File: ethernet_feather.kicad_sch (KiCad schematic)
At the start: 53 parts, among them J1 USB_C_Receptacle_USB2.0, J2 TC2030-NL, J3 JST PH 2 pin, J4 JST SH4 pin, J4 RJ45_Abracon_ARJM11D7-114-AB-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, J5 Conn_02x02_Odd_Even, U1 MIMXRT1051CVJ5B, U2 LP3982IMM-3.3, U3 MCP73831-2-OT, U4 W25Q32JVZP, U5 WE-TVS-82400102, Y1 24MHz 6pF, Y2 32.768kHz 7pF

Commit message: Finish PHY schematic (except capacitor values and component selection)
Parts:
- removed J?: Micro_SD_Card, symbol Connector:Micro_SD_Card
- added C26, C29: 100nF, symbol Device:C_Small
- added C27: 470pF, symbol Device:C_Small
- added C28: 1µF, symbol Device:C_Small
- added C30, C31: TODO, symbol Device:C_Small
- added FB1: FerriteBead_Small, symbol Device:FerriteBead_Small
- added R10, R11, R8, R9: 49.9Ω, symbol Device:R_Small
- added R12: 12.1kΩ 1%, symbol Device:R_Small
- added R13, R16, R17, R18, R24: 10kΩ, symbol Device:R_Small
- added R14, R15: 270Ω, symbol Device:R_Small
- added R19, R20, R21, R22, R23: 33Ω, symbol Device:R_Small
- added R25: 1.5kΩ, symbol Device:R_Small
- added U6: LAN8742A, Package_DFN_QFN:VQFN-24-1EP_4x4mm_P0.5mm_EP2.45x2.45mm_ThermalVias, symbol ethernet_feather:LAN8742A
- added U7: HSP061-4M10, ethernet_feather:ST_µQFN-10L, symbol ethernet_feather:HSP061-4M10
- added Y3: 25MHz, symbol Device:Crystal_GND24_Small
- C24: footprint Capacitor_SMD:C_0603_1608Metric -> (none)
- C25: renamed from C?; footprint (none) -> Capacitor_SMD:C_0603_1608Metric
- J5: value Conn_02x02_Odd_Even -> 2x2 header
- R6, R7: renamed from R?; footprint (none) -> Resistor_SMD:R_0603_1608Metric
- renumbered J4 to J6
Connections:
- net +3V3: now also C29.2, FB1.1, R16.1, R17.1, R18.1, R25.2, U6.9 (VDDIO)
- net GND: now also C24.2, C26.2, C27.2, C28.2, C29.1, C30.2, C31.2, R12.2, R13.2, R14.2, R15.2, R24.2, U6.25 (VSS), U7.3 (GND), U7.8 (GND), Y3.2, Y3.4; no longer C24.1
- net ENET_VDDA: now reaches J6.4 (CT)
- net ENET_VDDA: now also C23.2, C24.1, J6.9 (V+), C26.1, FB1.2, R10.1, R11.1, R8.1, R9.1, U6.1 (VDD2A), U6.19 (VDD1A); no longer C24.2
- net ENET_TX+: now reaches J6.10 (TD+)
- net ENET_TX+: now also R10.2, U6.21 (TXP), U7.4 (IO3), U7.7 (NC)
- net at J6.11 (RLED+): now also U6.3 (LED1/~{INT}/~{PME}/REGOFF)
- net at J6.12 (RLED-): now also R14.1
- net at J6.13 (LLED+): now also R13.1, U6.2 (LED2/~{INT}/~{PME}/~{INTSEL})
- net at J6.14 (LLED-): now also R15.1
- net ENET_RX-: now reaches J6.3 (RD+)
- net ENET_RX-: now also R9.2, U6.22 (RXN), U7.2 (IO2), U7.9 (NC)
- net ENET_RX+: now reaches J6.5 (CT)
- net ENET_RX+: now also R8.2, U6.23 (RXP), U7.1 (IO1), U7.10 (NC)
- net ENET_TX-: now reaches J6.8 (TD-)
- net ENET_TX-: now also R11.2, U6.20 (TXN), U7.5 (IO4), U7.6 (NC)
- new net: C27.1, C28.1, U6.6 (VDDCR)
- new net: R17.2, R20.2, U6.7 (RXD1/MODE1)
- new net: C30.1, U6.4 (XTAL2), Y3.1
- new net: R22.2, R24.1, U6.10 (RXER/PHYAD0)
- new net: R16.2, R21.2, U6.11 (CRS_DV/MODE2)
- new net: R18.2, R19.2, U6.8 (RXD0/MODE0)
- new net: R12.1, U6.24 (RBIAS)
- new net: C31.1, U6.5 (XTAL1/CLKIN), Y3.3
- new net: R23.2, U6.14 (~{INT}/REFCLK0)
- new net ENET_CRS_DV: R21.1
- new net ENET_MDC: U6.13 (MDC)
- new net ENET_MDIO: R25.1, U6.12 (MDIO)
- new net ENET_REFCLK: R23.1
- new net ENET_RXD0: R19.1
- new net ENET_RXD1: R20.1
- new net ENET_RXER: R22.1
- new net ENET_TXD0: U6.17 (TXD0)
- new net ENET_TXD1: U6.18 (TXD1)
- new net ENET_TXEN: U6.16 (TXEN)
- new net ENET_~{RST}: U6.15 (~{RST})
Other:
- moved on the sheet: J5, U1D, U1E

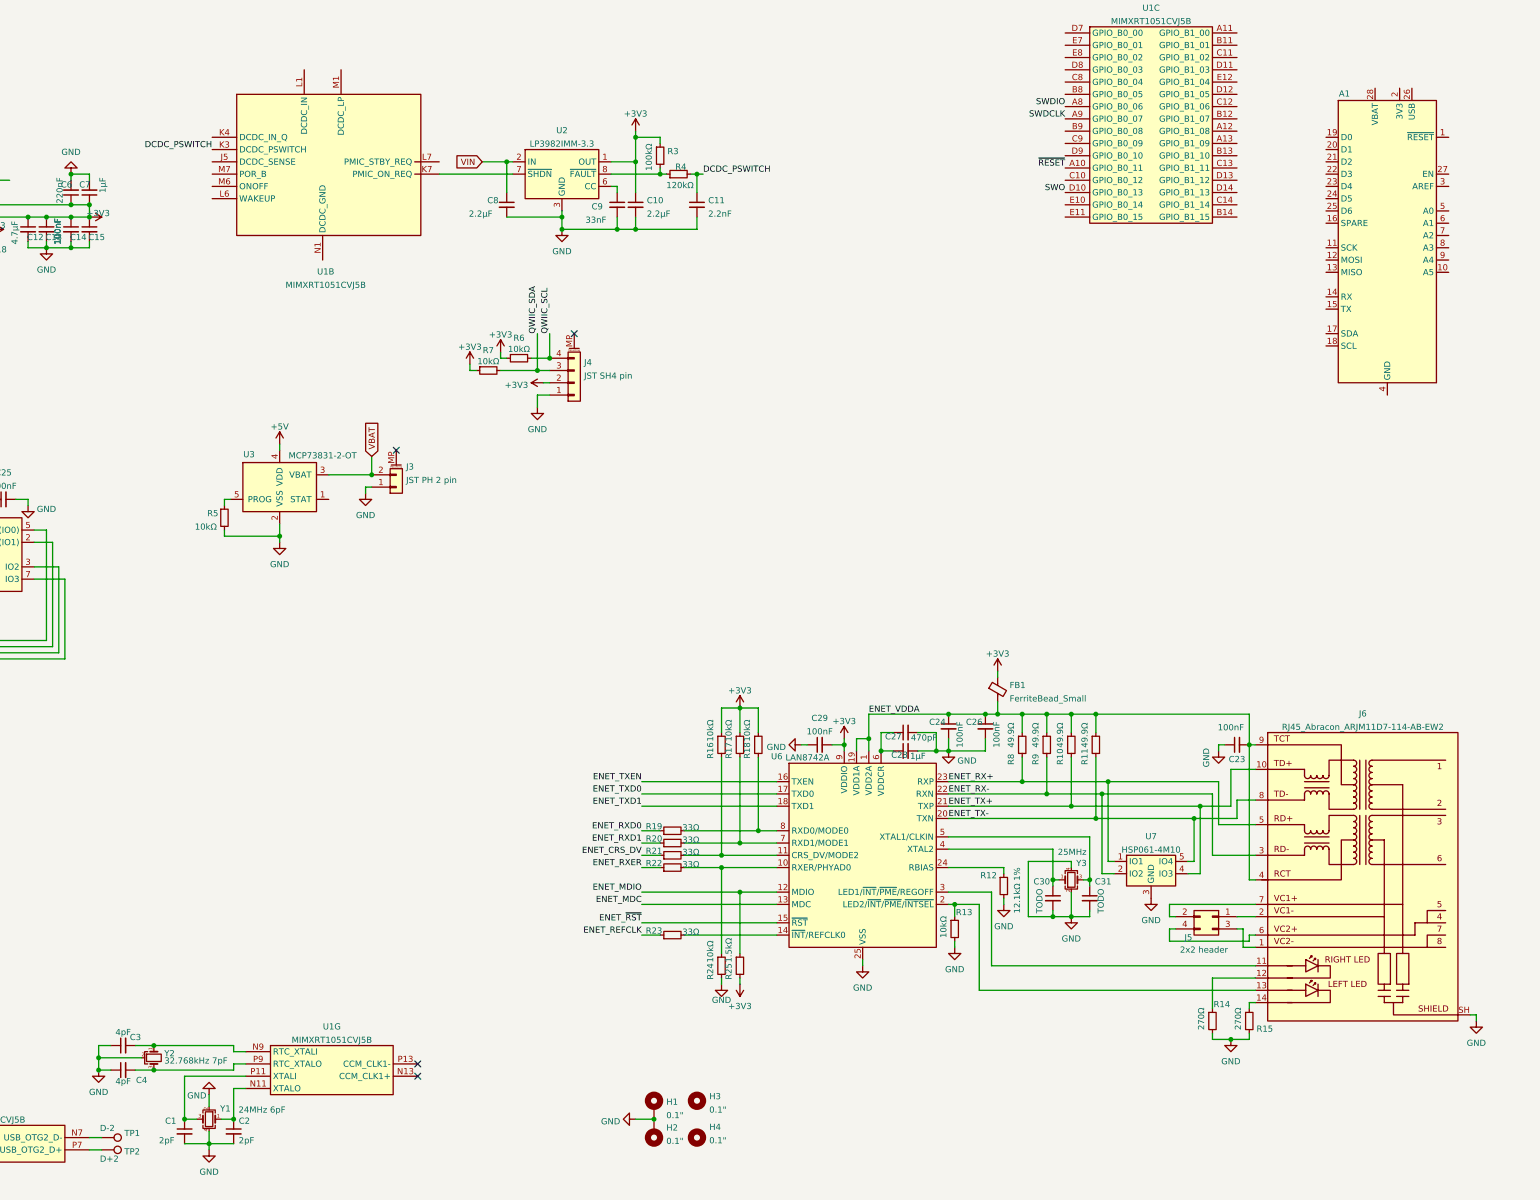
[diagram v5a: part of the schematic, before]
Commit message: Select crystals and resonance capacitors
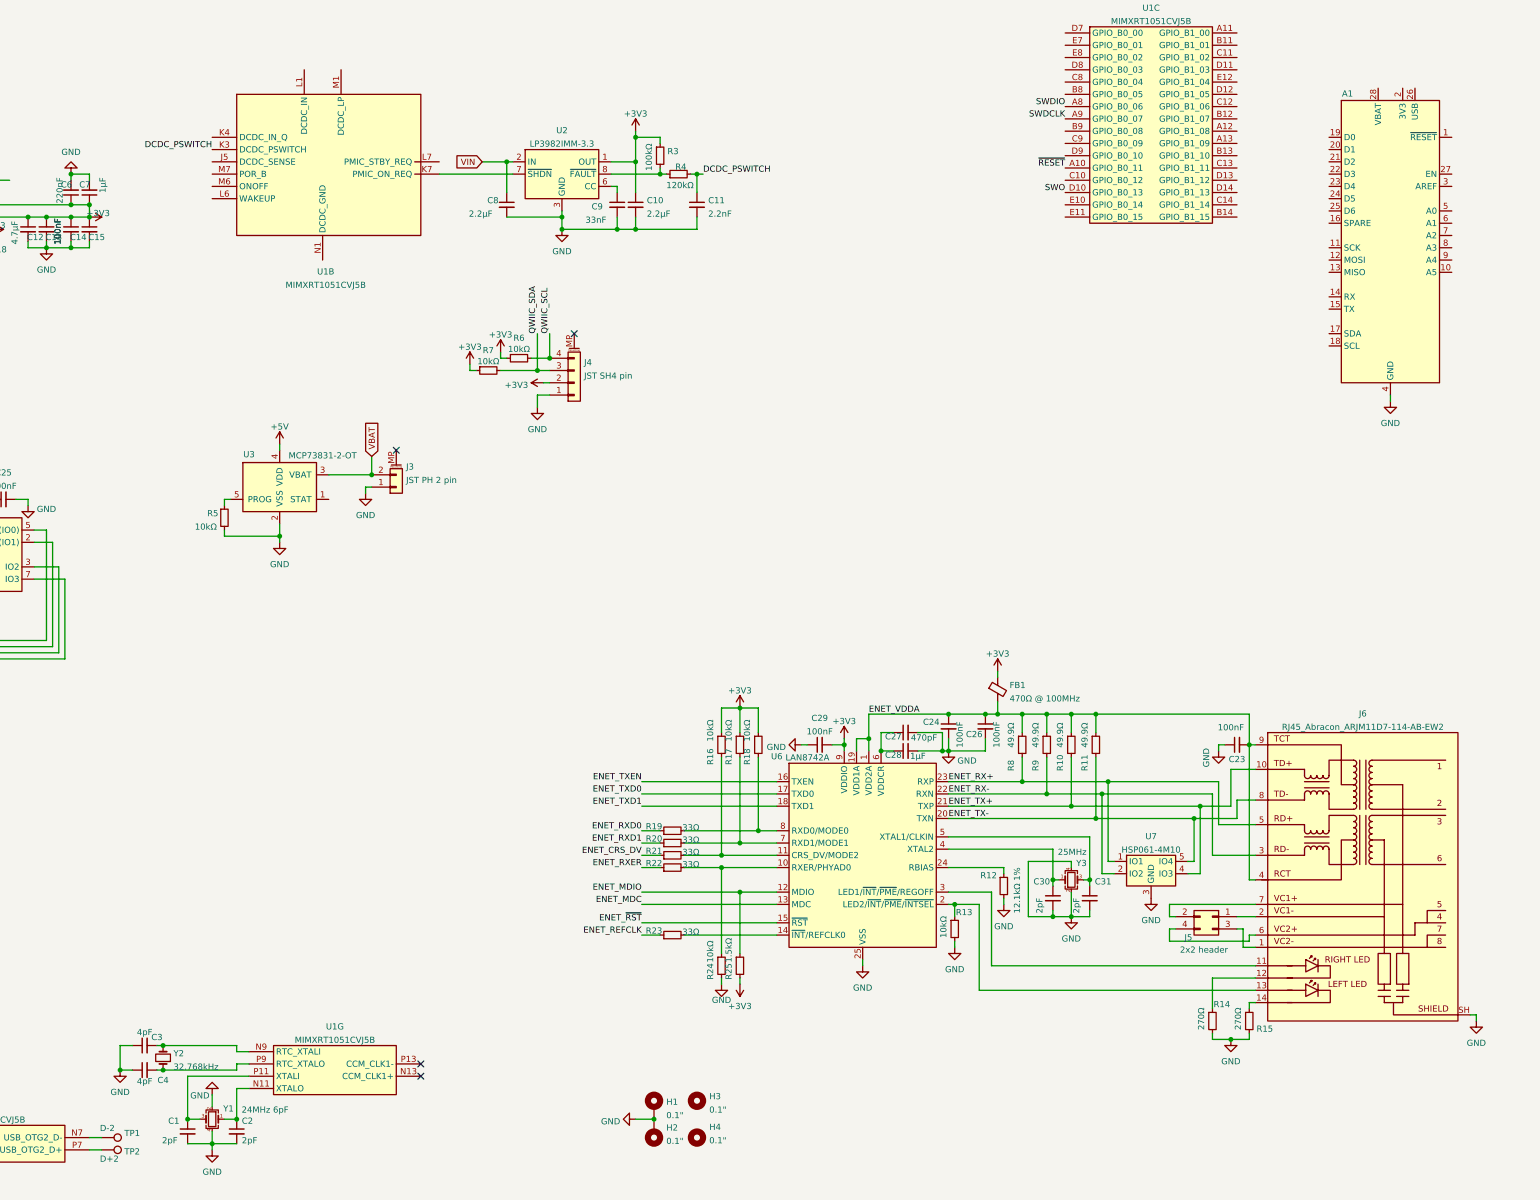
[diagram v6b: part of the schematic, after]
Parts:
- removed Y2: 32.768kHz 7pF, Crystal:Crystal_SMD_MicroCrystal_MS3V-T1R, symbol Device:Crystal_GND2_Small
- added Y2: 32.768kHz, Crystal:Crystal_SMD_2520-4Pin_2.5x2.0mm, symbol Device:Crystal_Small
- C30, C31: value TODO -> 2pF
- FB1: value FerriteBead_Small -> 470Ω @ 100MHz
- Y3: footprint (none) -> Crystal:Crystal_SMD_2016-4Pin_2.0x1.6mm
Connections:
- net GND: now also A1.4 (GND)
- net at C3.2, U1.N9 (RTC_XTALI): now also Y2.2
- net at C4.2, U1.P9 (RTC_XTALO): now also Y2.1
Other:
- moved on the sheet: A1, C1, C2, C3, C4, U1G, Y1

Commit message: Split out ethernet schematic
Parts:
- removed C12, C16, C19, C21: 4.7µF, Capacitor_SMD:C_0603_1608Metric, symbol Device:C_Small
- removed C13, C14, C15, C17, C18, C20, C22, C23: 100nF, Capacitor_SMD:C_0603_1608Metric, symbol Device:C_Small
- removed C24, C26, C29: 100nF, symbol Device:C_Small
- removed C27: 470pF, symbol Device:C_Small
- removed C28: 1µF, symbol Device:C_Small
- removed C30, C31: 2pF, symbol Device:C_Small
- removed C5: C_Small, Capacitor_SMD:C_0603_1608Metric, symbol Device:C_Small
- removed C6: 220nF, Capacitor_SMD:C_0603_1608Metric, symbol Device:C_Small
- removed C7: 1µF, Capacitor_SMD:C_0603_1608Metric, symbol Device:C_Small
- removed FB1: 470Ω @ 100MHz, symbol Device:FerriteBead_Small
- removed J5: 2x2 header, Connector_PinSocket_2.54mm:PinSocket_2x02_P2.54mm_Vertical, symbol Connector_Generic:Conn_02x02_Odd_Even
- removed J6: RJ45_Abracon_ARJM11D7-114-AB-EW2, ethernet_feather:RJ45_Abracon_ARJM11D7-114, symbol ethernet_feather:RJ45_Abracon_ARJM11D7-114-AB-EW2
- removed R10, R11, R8, R9: 49.9Ω, symbol Device:R_Small
- removed R12: 12.1kΩ 1%, symbol Device:R_Small
- removed R13, R16, R17, R18, R24: 10kΩ, symbol Device:R_Small
- removed R14, R15: 270Ω, symbol Device:R_Small
- removed R19, R20, R21, R22, R23: 33Ω, symbol Device:R_Small
- removed R25: 1.5kΩ, symbol Device:R_Small
- removed U6: LAN8742A, Package_DFN_QFN:VQFN-24-1EP_4x4mm_P0.5mm_EP2.45x2.45mm_ThermalVias, symbol ethernet_feather:LAN8742A
- removed U7: HSP061-4M10, ethernet_feather:ST_µQFN-10L, symbol ethernet_feather:HSP061-4M10
- removed Y3: 25MHz, Crystal:Crystal_SMD_2016-4Pin_2.0x1.6mm, symbol Device:Crystal_GND24_Small
- added C? (x19): 100nF, Capacitor_SMD:C_0603_1608Metric, symbol Device:C_Small
- added C? (x8): 4.7µF, Capacitor_SMD:C_0603_1608Metric, symbol Device:C_Small
- added C? (x4): 220nF, Capacitor_SMD:C_0603_1608Metric, symbol Device:C_Small
- added C?: 1µF, Capacitor_SMD:C_0603_1608Metric, symbol Device:C_Small
- added C?: 10µF, Capacitor_SMD:C_0603_1608Metric, symbol Device:C_Small
- added C? (x2): 220nF, symbol Device:C_Small
- added C?: 33µF, symbol Device:C_Small
- added D? (x2): BAS40-05, Package_TO_SOT_SMD:SOT-23, symbol Device:D_Schottky_Dual_CommonCathode_AAK_Parallel
- added L?: 4.7µH, symbol Device:L_Small
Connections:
- net +3V3: now also U1.P10 (NVCC_PLL), C?.1, C?.1, C?.1, C?.1, C?.1, C?.1, C?.1, C?.1, C?.1, C?.1, C?.1, C?.1, C?.1, C?.1, C?.1, C?.1, C?.1, D?.1 (K)
- net DCDC_IN: now also U1.K4 (DCDC_IN_Q)
- net GND: now also C?.2, C?.2, C?.2, C?.2, C?.2, C?.2, C?.2, C?.2, C?.2, C?.2, C?.2, C?.2, C?.2, C?.2, C?.2, C?.2, C?.2, C?.2, C?.2, C?.2, C?.2, C?.2, C?.2, C?.2, C?.2, C?.2, C?.2, C?.2, C?.2, C?.2, C?.2, C?.2, C?.2, C?.2, C?.2, C?.2
- net VBAT: now also D?.2 (K)
- net VUSB: now also U1.N6 (USB_OTG1_VBUS)
- net VDD_USB_CAP: now reaches U1.K8 (VDD_USB_CAP)
- net VDD_USB_CAP: now also C?.1, C?.1, D?.1 (K)
- net VDD_SNVS_CAP: now reaches U1.M10 (VDD_SNVS_CAP)
- net VDD_SNVS_CAP: now also C?.1
- net VDD_SNVS_IN: now reaches U1.M9 (VDD_SNVS_IN)
- net VDD_SNVS_IN: now also C?.1, D?.3 (A), D?.3 (A)
- net VDD_HIGH_CAP: now reaches U1.P8 (VDD_HIGH_CAP)
- net VDD_HIGH_CAP: now also C?.1, C?.1
- net at U1.M1 (DCDC_LP), U1.M2 (DCDC_LP): now also L?.2
- net VDD_SOC_IN renamed +1V1
- net +1V1: now also C?.1, C?.1, C?.1, C?.1, C?.1, C?.1, C?.1, C?.1, C?.1, C?.1, C?.1, C?.1, C?.1, L?.1
- no-connect marks 6 -> 9
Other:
- added sheet Ethernet (enet.kicad_sch)
- note added: "This is against spec but i don't care"
- moved on the sheet: C10, C11, C8, C9, H1, H2, H3, H4, J3, J4, R3, R4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

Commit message: Some PSU changes, add new solder jumper symbol
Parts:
- removed C?: 220nF, symbol Device:C_Small
- removed D? (x2): BAS40-05, Package_TO_SOT_SMD:SOT-23, symbol Device:D_Schottky_Dual_CommonCathode_AAK_Parallel
- added C?: 220nF, Capacitor_SMD:C_0603_1608Metric, symbol Device:C_Small
- added D?: D_Schottky, symbol Device:D_Schottky
- added JP?: SolderJumper_3_Bridged123, ethernet_feather:SolderJumper-3_P1.3mm_Bridged123_RoundedPad1.0x1.5mm, symbol Jumper:SolderJumper_3_Bridged123
- added Q?: Q_PMOS_DGS, symbol Device:Q_PMOS_DGS
- added R?: 10kΩ, symbol Device:R_Small
- added TP?: TestPoint, symbol Connector:TestPoint
- R1, R2: value 5.6kΩ -> 5.1kΩ
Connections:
- net +5V is gone; now on net VUSB: U3.4 (VDD)
- net GND is gone; now on net DCDC_GND: A1.4 (GND), C1.2, C10.2, C11.2, C2.2, C25.2, C3.1, C4.1, C8.2, C9.2, C?.2, C?.2, C?.2, C?.2, C?.2, C?.2, C?.2, C?.2, C?.2, C?.2, C?.2, C?.2, C?.2, C?.2, C?.2, C?.2, C?.2, C?.2, C?.2, C?.2, C?.2, C?.2, C?.2, C?.2, C?.2, C?.2, C?.2, C?.2, C?.2, C?.2, C?.2, C?.2, C?.2, C?.2, C?.2, H1.1, H2.1, J1.A1 (GND), J1.A12 (GND), J1.B1 (GND), J1.B12 (GND), J1.S1 (SHIELD), J2.5 (Pin_5), J3.1 (Pin_1), J4.1 (Pin_1), R1.2, R2.2, R5.2, U1.A1 (VSS), U1.A14 (VSS), U1.B10 (VSS), U1.B5 (VSS), U1.E13 (VSS), U1.E2 (VSS), U1.G7 (VSS), U1.G8 (VSS), U1.H7 (VSS), U1.H8 (VSS), U1.J7 (VSS), U1.J8 (VSS), U1.K13 (VSS), U1.K2 (VSS), U1.K9 (NGND_KEL0), U1.L9 (VSS), U1.N5 (VSS), U1.N8 (VSS), U1.P1 (VSS), U1.P14 (VSS), U2.3 (GND), U3.2 (VSS), U4.4 (GND), U4.9 (EP), U5.2, Y1.2, Y1.4
- net VDD_SNVS_IN is gone; now on net +3V3: U1.M9 (VDD_SNVS_IN)
- net +1V1: now also U1.J5 (DCDC_SENSE)
- net +3V3: now also C?.1, JP?.2 (C); no longer R6.1, R7.1
- net DCDC_GND: now also C?.2, R?.2
- net VBAT: now also Q?.1 (D)
- net VIN: now also U2.7 (~{SHDN}), D?.1 (K), Q?.3 (S)
- net VUSB: now also D?.2 (A), Q?.2 (G), R?.1
- net ENET_~{RST}: now reaches U1.A2 (GPIO_EMC_27)
- net ENET_RXD0: now reaches U1.A3 (GPIO_EMC_20)
- net ENET_MDC: now reaches U1.A7 (GPIO_EMC_40)
- net ENET_RXER: now reaches U1.B3 (GPIO_EMC_26)
- net ENET_RXD1: now reaches U1.B4 (GPIO_EMC_19)
- net ENET_TXD1: now reaches U1.C1 (GPIO_EMC_21)
- net ENET_MDIO: now reaches U1.C7 (GPIO_EMC_41)
- net ENET_REFCLK: now reaches U1.D2 (GPIO_EMC_25)
- net ENET_TXEN: now reaches U1.D3 (GPIO_EMC_24)
- net ENET_TXD0: now reaches U1.F1 (GPIO_EMC_22)
- net ENET_CRS_DV: now reaches U1.G2 (GPIO_EMC_23)
- net at U1.K7 (PMIC_ON_REQ): no longer U2.7 (~{SHDN})
- net DCDC_PSWITCH: no longer names the net of C11.1, R4.2, U1.K3 (DCDC_PSWITCH)
- net DCDC_PSWITCH: now also TP?.1
- new net: JP?.3 (B), R6.1
- new net: JP?.1 (A), R7.1
- no-connect marks 9 -> 12
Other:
- note removed: "This is against spec but i don't care"
- moved on the sheet: C10, C11, C8, C9, C?, H1, H2, H3, H4, J3, L?, R3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
